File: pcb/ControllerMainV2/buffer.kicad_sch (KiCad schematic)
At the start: 22 parts, among them IC4 AD5293BRUZ-20-RL7, IC5 AD5293BRUZ-20-RL7, U3 TL074

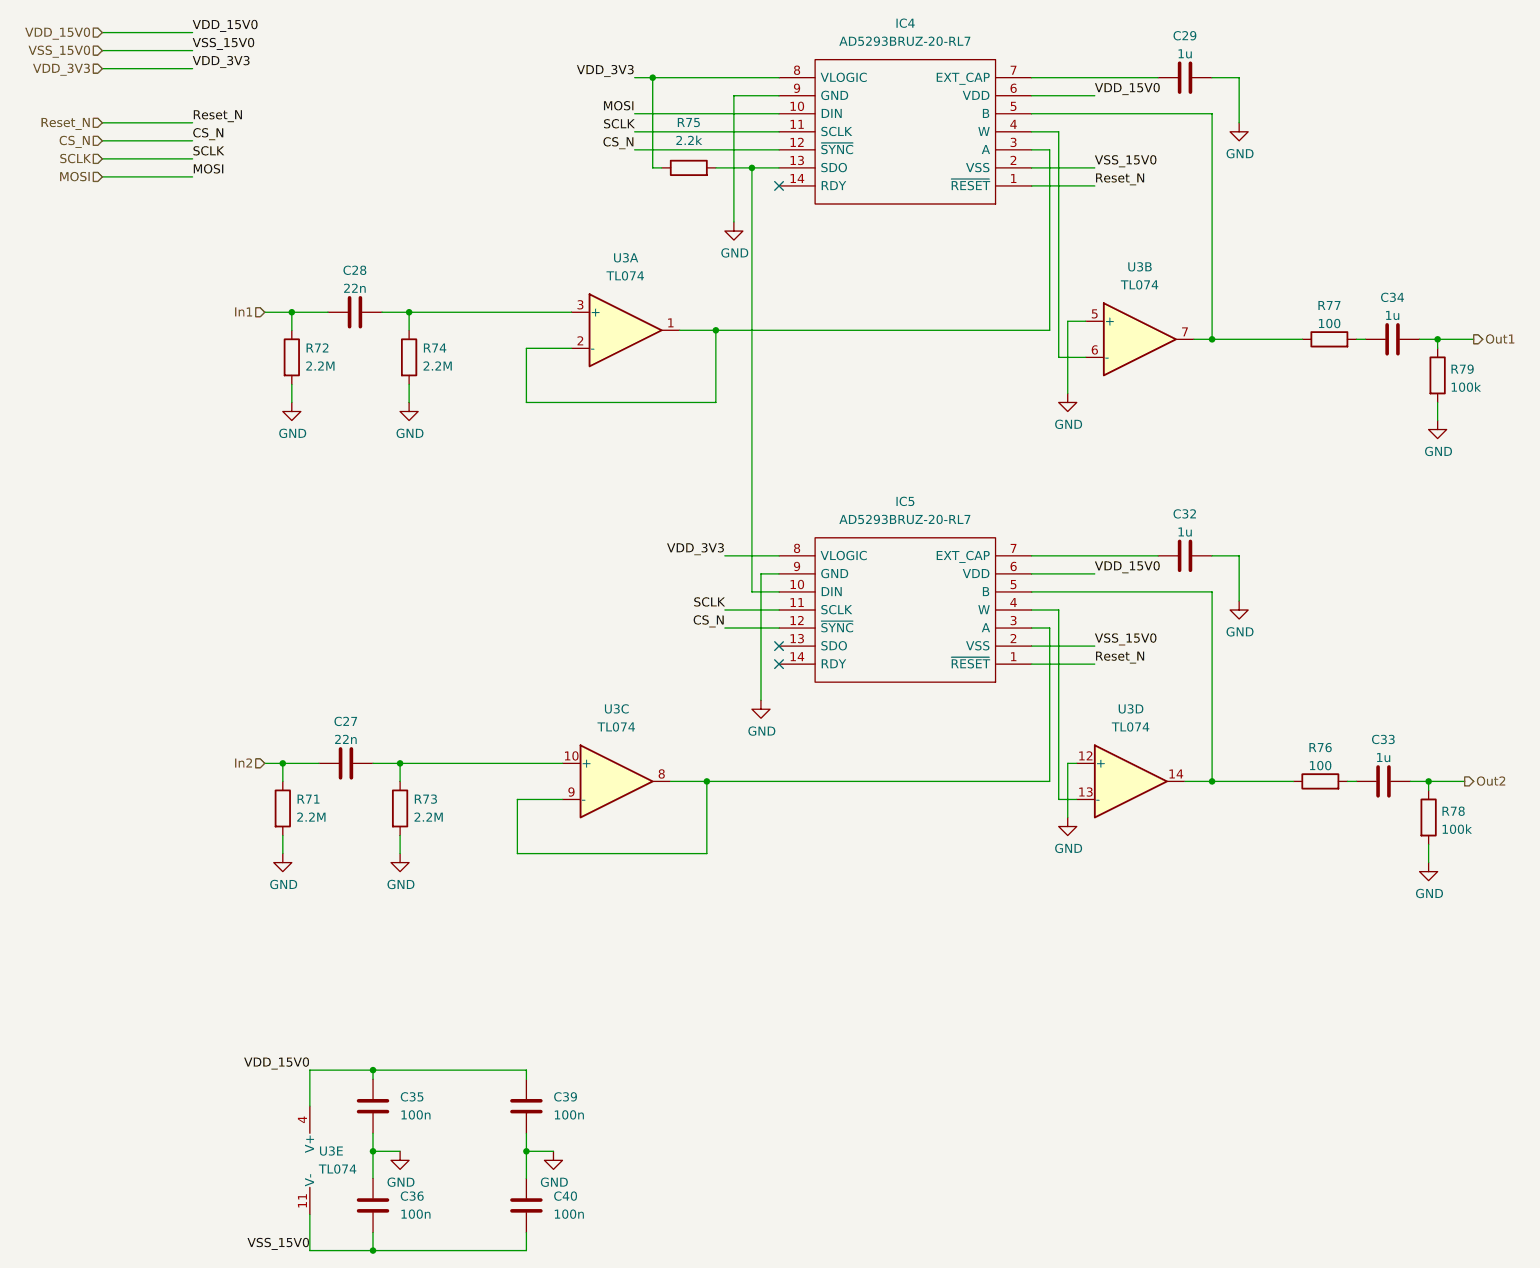
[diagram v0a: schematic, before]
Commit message: New version with smaller enclosure
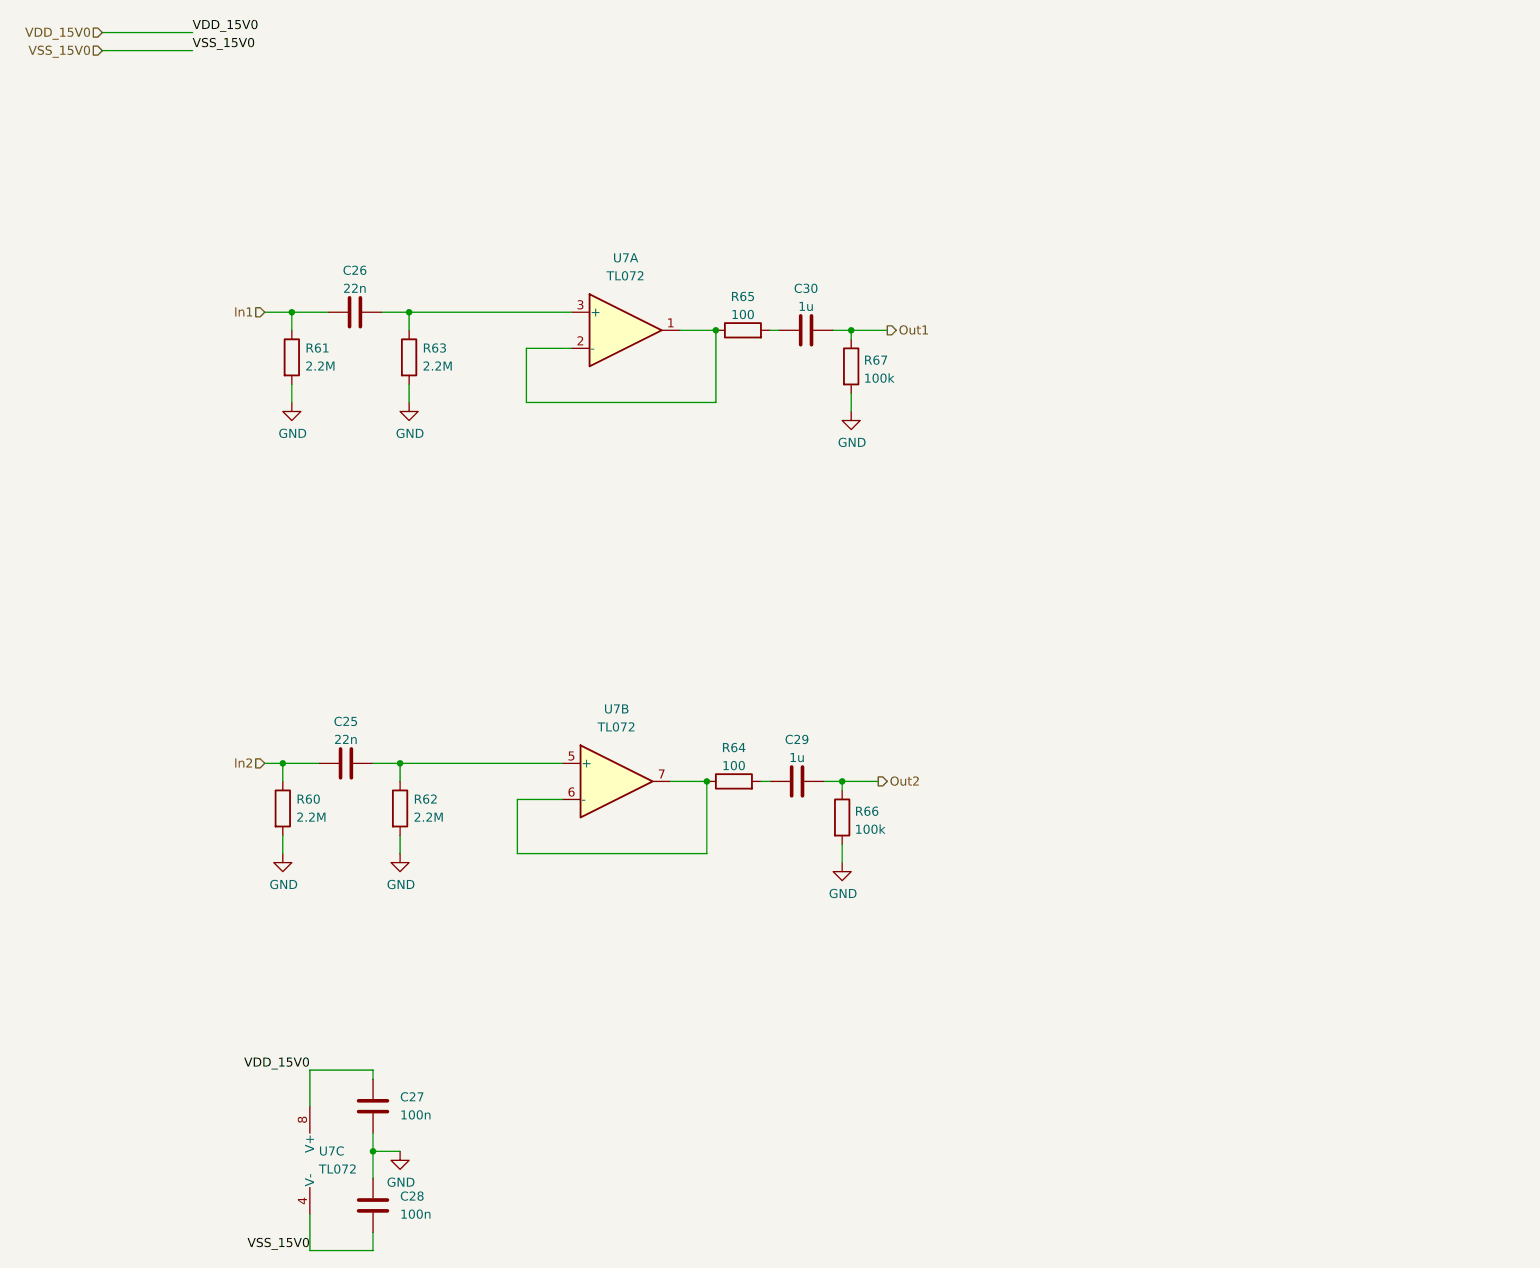
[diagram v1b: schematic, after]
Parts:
- removed C29, C32: 1u, Capacitor_SMD:C_1206_3216Metric_Pad1.33x1.80mm_HandSolder, symbol Device:C
- removed C35, C36, C39, C40: 100n, Capacitor_SMD:C_1206_3216Metric_Pad1.33x1.80mm_HandSolder, symbol Device:C
- removed IC4, IC5: AD5293BRUZ-20-RL7, SamacSys_Parts:SOP65P640X120-14N, symbol SamacSys_Parts:AD5293BRUZ-20-RL7
- removed R75: 2.2k, Resistor_SMD:R_1206_3216Metric_Pad1.30x1.75mm_HandSolder, symbol Device:R
- removed U3: TL074, SamacSys_Parts:SOIC127P600X175-14N, symbol Amplifier_Operational:TL074
- added C27, C28: 100n, Capacitor_SMD:C_1206_3216Metric_Pad1.33x1.80mm_HandSolder, symbol Device:C
- added U7: TL072, Package_SO:SOIC-8_3.9x4.9mm_P1.27mm, symbol Amplifier_Operational:TL072
- R60: renamed from R71; footprint Resistor_SMD:R_1206_3216Metric_Pad1.30x1.75mm_HandSolder -> Resistor_SMD:R_0805_2012Metric_Pad1.20x1.40mm_HandSolder
- R61: renamed from R72; footprint Resistor_SMD:R_1206_3216Metric_Pad1.30x1.75mm_HandSolder -> Resistor_SMD:R_0805_2012Metric_Pad1.20x1.40mm_HandSolder
- R62: renamed from R73; footprint Resistor_SMD:R_1206_3216Metric_Pad1.30x1.75mm_HandSolder -> Resistor_SMD:R_0805_2012Metric_Pad1.20x1.40mm_HandSolder
- R63: renamed from R74; footprint Resistor_SMD:R_1206_3216Metric_Pad1.30x1.75mm_HandSolder -> Resistor_SMD:R_0805_2012Metric_Pad1.20x1.40mm_HandSolder
- R64: renamed from R76; footprint Resistor_SMD:R_1206_3216Metric_Pad1.30x1.75mm_HandSolder -> Resistor_SMD:R_0805_2012Metric_Pad1.20x1.40mm_HandSolder
- R65: renamed from R77; footprint Resistor_SMD:R_1206_3216Metric_Pad1.30x1.75mm_HandSolder -> Resistor_SMD:R_0805_2012Metric_Pad1.20x1.40mm_HandSolder
- R66: renamed from R78; footprint Resistor_SMD:R_1206_3216Metric_Pad1.30x1.75mm_HandSolder -> Resistor_SMD:R_0805_2012Metric_Pad1.20x1.40mm_HandSolder
- R67: renamed from R79; footprint Resistor_SMD:R_1206_3216Metric_Pad1.30x1.75mm_HandSolder -> Resistor_SMD:R_0805_2012Metric_Pad1.20x1.40mm_HandSolder
- renumbered C27 to C25, C28 to C26, C33 to C29, C34 to C30
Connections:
- net GND: now also C27.1, C28.2
- net VDD_15V0: now also C27.2, U7.8 (V+)
- net VSS_15V0: now also C28.1, U7.4 (V-)
- net at R64.1: now also U7.6 (-), U7.7
- net at C25.2, R62.1: now also U7.5 (+)
- net at R65.1: now also U7.1, U7.2 (-)
- net at C26.2, R63.1: now also U7.3 (+)
- no-connect marks 3 -> 0
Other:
- moved on the sheet: C29, C30, R64, R65, R66, R67
